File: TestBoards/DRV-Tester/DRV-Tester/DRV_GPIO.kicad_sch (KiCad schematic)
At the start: 1 part, among them J7 Conn_02x04_Odd_Even

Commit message: update tester board with layout
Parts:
- added J12: Conn_02x04_Odd_Even, Connector_PinHeader_2.54mm:PinHeader_2x04_P2.54mm_Vertical, symbol Connector_Generic:Conn_02x04_Odd_Even
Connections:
- net 3v3_VCC: now also J12.8 (Pin_8)
- net GND: now also J12.2 (Pin_2)
- new net IPROPI2: J12.4 (Pin_4)
- new net N_FAULT2: J12.6 (Pin_6)
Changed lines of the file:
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@@
+	(wire
+		(pts
+			(xy 130.81 76.2) (xy 134.62 76.2)
+		)
+		(stroke
+			(width 0)
+			(type default)
+		)
+	)
 	(wire
 		(pts
@@
 		)
 	)
+	(wire
+		(pts
+			(xy 130.81 73.66) (xy 134.62 73.66)
+		)
+		(stroke
+			(width 0)
+			(type default)
+		)
+	)
 	(bus
 		(pts
@@
 	(wire
 		(pts
+			(xy 130.81 78.74) (xy 134.62 78.74)
+		)
+		(stroke
+			(width 0)
+			(type default)
+		)
+	)
+	(wire
+		(pts
 			(xy 113.03 60.96) (xy 118.11 60.96)
 		)
@@
 		(pts
 			(xy 90.17 60.96) (xy 86.36 60.96)
+		)
+		(stroke
+			(width 0)
+			(type default)
+		)
+	)
+	(wire
+		(pts
+			(xy 130.81 71.12) (xy 139.7 71.12)
 		)
 		(stroke
@@
 			)
 			(justify right bottom)
+		)
+	)
+	(hierarchical_label "3v3_VCC"
+		(shape input)
+		(at 134.62 78.74 0)
+		(fields_autoplaced yes)
+		(effects
+			(font
+				(size 1.27 1.27)
+			)
+			(justify left)
 		)
 	)
@@
 		)
 	)
+	(hierarchical_label "N_FAULT2"
+		(shape input)
+		(at 134.62 76.2 0)
+		(fields_autoplaced yes)
+		(effects
+			(font
+				(size 1.27 1.27)
+			)
+			(justify left)
+		)
+	)
 	(hierarchical_label "IPROPI"
 		(shape input)
 		(at 134.62 55.88 0)
+		(fields_autoplaced yes)
+		(effects
+			(font
+				(size 1.27 1.27)
+			)
+			(justify left)
+		)
+	)
+	(hierarchical_label "IPROPI2"
+		(shape input)
+		(at 134.62 73.66 0)
 		(fields_autoplaced yes)
 		(effects
@@
 		(instances
 			(project "DRV-Tester"
+				(path "/a38efaf2-f631-4fae-9db8-baf53fe35d9e/0f578a30-e239-4bae-9542-26272a6b03ce"
+					(reference "J9")
+					(unit 1)
+				)
+				(path "/a38efaf2-f631-4fae-9db8-baf53fe35d9e/97323246-a63b-4ba9-8e83-e2e6b5d34014"
+					(reference "J8")
+					(unit 1)
+				)
 				(path "/a38efaf2-f631-4fae-9db8-baf53fe35d9e/d91062bd-db31-49b8-8300-3058fb4afebc"
 					(reference "J7")
-					(unit 1)
-				)
-				(path "/a38efaf2-f631-4fae-9db8-baf53fe35d9e/0f578a30-e239-4bae-9542-26272a6b03ce"
-					(reference "J9")
-					(unit 1)
-				)
-				(path "/a38efaf2-f631-4fae-9db8-baf53fe35d9e/97323246-a63b-4ba9-8e83-e2e6b5d34014"
-					(reference "J8")
 					(unit 1)
 				)
@@
 		(instances
 			(project "DRV-Tester"
+				(path "/a38efaf2-f631-4fae-9db8-baf53fe35d9e/0f578a30-e239-4bae-9542-26272a6b03ce"
+					(reference "#PWR019")
+					(unit 1)
+				)
+				(path "/a38efaf2-f631-4fae-9db8-baf53fe35d9e/97323246-a63b-4ba9-8e83-e2e6b5d34014"
+					(reference "#PWR017")
+					(unit 1)
+				)
 				(path "/a38efaf2-f631-4fae-9db8-baf53fe35d9e/d91062bd-db31-49b8-8300-3058fb4afebc"
 					(reference "#PWR018")
 					(unit 1)
 				)
+			)
+		)
+	)
+	(symbol
+		(lib_id "power:GND")
+		(at 139.7 71.12 90)
+		(unit 1)
+		(exclude_from_sim no)
+		(in_bom yes)
+		(on_board yes)
+		(dnp no)
+		(fields_autoplaced yes)
+		(property "Reference" "#PWR026"
+			(at 146.05 71.12 0)
+			(effects
+				(font
+					(size 1.27 1.27)
+				)
+				(hide yes)
+			)
+		)
+		(property "Value" "GND"
+			(at 143.51 71.1199 90)
+			(effects
+				(font
+					(size 1.27 1.27)
+				)
+				(justify right)
+			)
+		)
+		(property "Footprint" ""
+			(at 139.7 71.12 0)
+			(effects
+				(font
+					(size 1.27 1.27)
+				)
+				(hide yes)
+			)
+		)
+		(property "Datasheet" ""
+			(at 139.7 71.12 0)
+			(effects
+				(font
+					(size 1.27 1.27)
+				)
+				(hide yes)
+			)
+		)
+		(property "Description" "Power symbol creates a global label with name \"GND\" , ground"
+			(at 139.7 71.12 0)
+			(effects
+				(font
+					(size 1.27 1.27)
+				)
+				(hide yes)
+			)
+		)
+		(pin "1"
+		)
+		(instances
+			(project "DRV-Tester"
 				(path "/a38efaf2-f631-4fae-9db8-baf53fe35d9e/0f578a30-e239-4bae-9542-26272a6b03ce"
-					(reference "#PWR019")
+					(reference "#PWR028")
 					(unit 1)
 				)
 				(path "/a38efaf2-f631-4fae-9db8-baf53fe35d9e/97323246-a63b-4ba9-8e83-e2e6b5d34014"
-					(reference "#PWR017")
-					(unit 1)
-				)
+					(reference "#PWR026")
+					(unit 1)
+				)
+				(path "/a38efaf2-f631-4fae-9db8-baf53fe35d9e/d91062bd-db31-49b8-8300-3058fb4afebc"
+					(reference "#PWR027")
+					(unit 1)
+				)
+			)
+		)
+	)
+	(symbol
+		(lib_id "Connector_Generic:Conn_02x04_Odd_Even")
+		(at 123.19 73.66 0)
+		(unit 1)
+		(exclude_from_sim no)
+		(in_bom yes)
+		(on_board yes)
+		(dnp no)
+		(fields_autoplaced yes)
+		(property "Reference" "J12"
+			(at 124.46 64.77 0)
+			(effects
+				(font
+					(size 1.27 1.27)
+				)
+			)
+		)
+		(property "Value" "Conn_02x04_Odd_Even"
+			(at 124.46 67.31 0)
+			(effects
+				(font
+					(size 1.27 1.27)
+				)
+			)
+		)
+		(property "Footprint" "Connector_PinHeader_2.54mm:PinHeader_2x04_P2.54mm_Vertical"
+			(at 123.19 73.66 0)
+			(effects
+				(font
+					(size 1.27 1.27)
+				)
+				(hide yes)
+			)
+		)
+		(property "Datasheet" "~"
+			(at 123.19 73.66 0)
+			(effects
+				(font
+					(size 1.27 1.27)
+				)
+				(hide yes)
+			)
+		)
+		(property "Description" "Generic connector, double row, 02x04, odd/even pin numbering scheme (row 1 odd numbers, row 2 even numbers), script generated (kicad-library-utils/schlib/autogen/connector/)"
+			(at 123.19 73.66 0)
+			(effects
+				(font
+					(size 1.27 1.27)
+				)
+				(hide yes)
+			)
+		)
+		(pin "6"
+		)
+		(pin "4"
+		)
+		(pin "7"
+		)
+		(pin "2"
+		)
+		(pin "5"
+		)
+		(pin "8"
+		)
+		(pin "1"
+		)
+		(pin "3"
+		)
+		(instances
+			(project "DRV-Tester"
+				(path "/a38efaf2-f631-4fae-9db8-baf53fe35d9e/0f578a30-e239-4bae-9542-26272a6b03ce"
+					(reference "J14")
+					(unit 1)
+				)
+				(path "/a38efaf2-f631-4fae-9db8-baf53fe35d9e/97323246-a63b-4ba9-8e83-e2e6b5d34014"
+					(reference "J12")
+					(unit 1)
+				)
+				(path "/a38efaf2-f631-4fae-9db8-baf53fe35d9e/d91062bd-db31-49b8-8300-3058fb4afebc"
+					(reference "J13")
+					(unit 1)
+				)

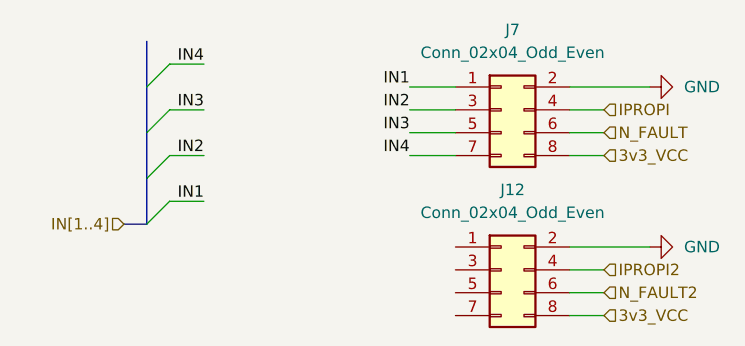
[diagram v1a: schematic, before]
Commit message: add caps and LEDs to testboard
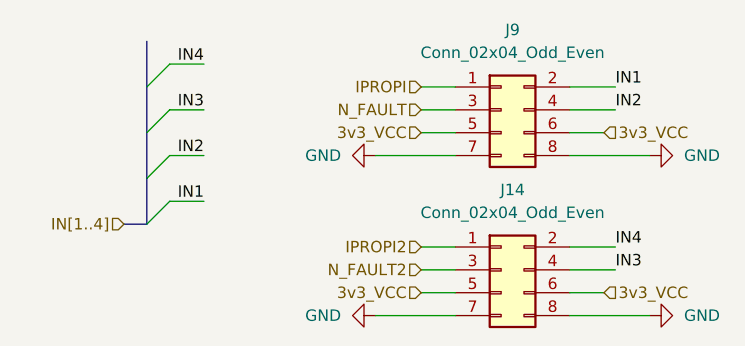
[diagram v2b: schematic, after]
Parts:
- renumbered J12 to J14, J7 to J9
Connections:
- net 3v3_VCC: now also J14.5 (Pin_5), J14.6 (Pin_6), J9.5 (Pin_5), J9.6 (Pin_6); no longer J14.8 (Pin_8), J9.8 (Pin_8)
- net GND: now also J14.7 (Pin_7), J14.8 (Pin_8), J9.7 (Pin_7), J9.8 (Pin_8); no longer J14.2 (Pin_2), J9.2 (Pin_2)
- net IN1: now also J9.2 (Pin_2); no longer J9.1 (Pin_1)
- net IN2: now also J9.4 (Pin_4); no longer J9.3 (Pin_3)
- net IN3: now also J14.4 (Pin_4); no longer J9.5 (Pin_5)
- net IN4: now also J14.2 (Pin_2); no longer J9.7 (Pin_7)
- net IPROPI: now also J9.1 (Pin_1); no longer J9.4 (Pin_4)
- net IPROPI2: now also J14.1 (Pin_1); no longer J14.4 (Pin_4)
- net N_FAULT: now also J9.3 (Pin_3); no longer J9.6 (Pin_6)
- net N_FAULT2: now also J14.3 (Pin_3); no longer J14.6 (Pin_6)
